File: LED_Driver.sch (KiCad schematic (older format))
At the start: 6 parts, among them U2 AP5726

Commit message: Back-annotated footprints into the schematic
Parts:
- C1, C2: footprint (none) -> Capacitors_SMD:c_0805
- D3: footprint (none) -> BenchBudEE:SOD-323
- L1: footprint (none) -> BenchBudEE:NR4012
- R7: footprint (none) -> SMD_Packages:SM0805
- U2: footprint (none) -> SMD_Packages:SOT23_6
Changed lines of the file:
@@
 F 0 "U2" H 4450 1950 60  0000 C CNN
 F 1 "AP5726" H 4100 2300 60  0000 C CNN
-F 2 "" H 4100 2300 60  0000 C CNN
+F 2 "SMD_Packages:SOT23_6" H 4100 2300 60  0001 C CNN
 F 3 "" H 4100 2300 60  0000 C CNN
 	1    4100 2300
@@
 F 0 "C1" H 3200 1500 40  0000 L CNN
 F 1 "1u" H 3206 1315 40  0000 L CNN
-F 2 "" H 3238 1250 30  0000 C CNN
+F 2 "Capacitors_SMD:c_0805" H 3238 1250 30  0001 C CNN
 F 3 "" H 3200 1400 60  0000 C CNN
 	1    3200 1400
@@
 F 0 "C2" H 8500 1500 40  0000 L CNN
 F 1 "1u" H 8506 1315 40  0000 L CNN
-F 2 "" H 8538 1250 30  0000 C CNN
+F 2 "Capacitors_SMD:c_0805" H 8538 1250 30  0001 C CNN
 F 3 "" H 8500 1400 60  0000 C CNN
 	1    8500 1400
@@
 F 0 "L1" V 4350 1000 40  0000 C CNN
 F 1 "22u" V 4500 1000 40  0000 C CNN
-F 2 "" H 4400 1000 60  0000 C CNN
+F 2 "BenchBudEE:NR4012" H 4400 1000 60  0001 C CNN
 F 3 "" H 4400 1000 60  0000 C CNN
 F 4 "NR4012T220M" H 4400 1000 60  0001 C CNN "MFG Part Number"
@@
 F 0 "D3" H 5600 1100 40  0000 C CNN
 F 1 "BO540WS-7" H 5600 900 40  0000 C CNN
-F 2 "" H 5600 1000 60  0000 C CNN
+F 2 "BenchBudEE:SOD-323" H 5600 1000 60  0001 C CNN
 F 3 "" H 5600 1000 60  0000 C CNN
 F 4 "BO540WS-7" H 5600 1000 60  0001 C CNN "MFG Part Number"
@@
 F 0 "R7" V 5380 2750 40  0000 C CNN
 F 1 "15" V 5307 2751 40  0000 C CNN
-F 2 "" V 5230 2750 30  0000 C CNN
+F 2 "SMD_Packages:SM0805" V 5230 2750 30  0001 C CNN
 F 3 "" H 5300 2750 30  0000 C CNN
 	1    5300 2750

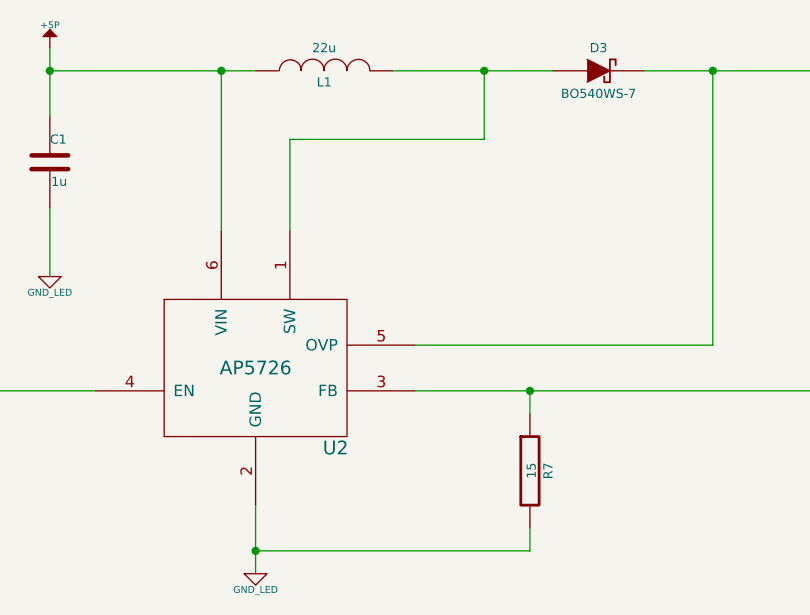
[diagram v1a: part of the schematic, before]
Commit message: Final part numbers added to schematic, cross-checked KiCAD BOM against manual BOM
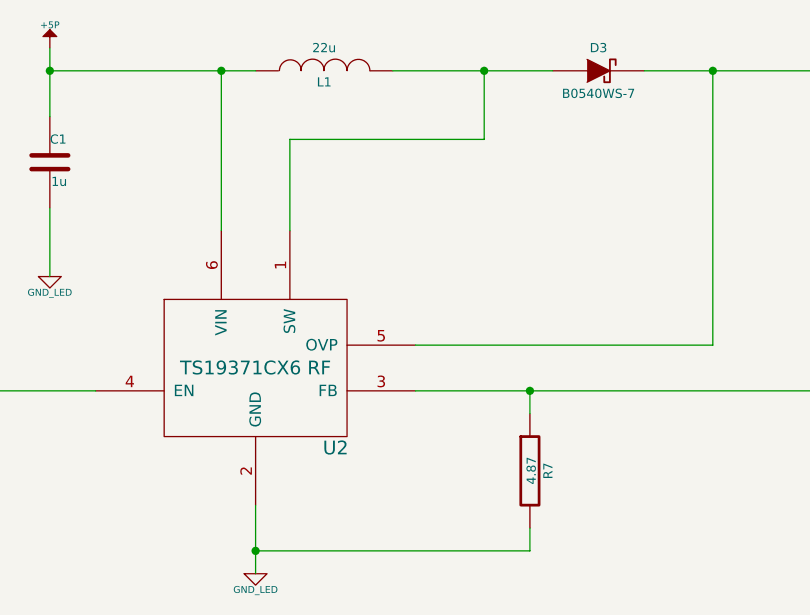
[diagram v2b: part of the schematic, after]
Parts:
- D3: value BO540WS-7 -> B0540WS-7
- R7: value 15 -> 4.87
- U2: value AP5726 -> TS19371CX6 RF
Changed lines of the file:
@@
 P 4100 2300
 F 0 "U2" H 4450 1950 60  0000 C CNN
-F 1 "AP5726" H 4100 2300 60  0000 C CNN
+F 1 "TS19371CX6 RF" H 4100 2300 60  0000 C CNN
 F 2 "SMD_Packages:SOT23_6" H 4100 2300 60  0001 C CNN
 F 3 "" H 4100 2300 60  0000 C CNN
@@
 P 5600 1000
 F 0 "D3" H 5600 1100 40  0000 C CNN
-F 1 "BO540WS-7" H 5600 900 40  0000 C CNN
+F 1 "B0540WS-7" H 5600 900 40  0000 C CNN
 F 2 "BenchBudEE:SOD-323" H 5600 1000 60  0001 C CNN
 F 3 "" H 5600 1000 60  0000 C CNN
@@
 P 5300 2750
 F 0 "R7" V 5380 2750 40  0000 C CNN
-F 1 "15" V 5307 2751 40  0000 C CNN
+F 1 "4.87" V 5307 2751 40  0000 C CNN
 F 2 "SMD_Packages:SM0805" V 5230 2750 30  0001 C CNN
 F 3 "" H 5300 2750 30  0000 C CNN
